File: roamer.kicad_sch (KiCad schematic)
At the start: 1 part

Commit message: Adding testpoints to I2C, SPI, and signals
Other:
- added sheet Bus - SPI (bus-spi.kicad_sch)
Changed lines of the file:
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@@
+	)
+	(sheet
+		(at 234.95 45.72)
+		(size 12.7 15.24)
+		(stroke
+			(width 0.1524)
+			(type solid)
+		)
+		(fill
+			(color 0 0 0 0.0000)
+		)
+		(property "Sheetname" "Bus - SPI"
+			(at 235.966 44.958 0)
+			(effects
+				(font
+					(size 1.27 1.27)
+				)
+				(justify left bottom)
+			)
+		)
+		(property "Sheetfile" "bus-spi.kicad_sch"
+			(at 248.2346 60.96 90)
+			(effects
+				(font
+					(size 1.27 1.27)
+				)
+				(justify left top)
+				(hide yes)
+			)
+		)
+		(pin "I2C{SCL SDA}" bidirectional
+			(at 241.3 60.96 270)
+			(effects
+				(font
+					(size 1.27 1.27)
+				)
+				(justify left)
+			)
+		)
+		(instances
+			(project "roamer"
+				(path "/1c59de6a-87fe-4223-8898-4b0383164a31"
+					(page "17")
+				)
+			)
+		)
 	)
 	(sheet

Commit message: Fixing lots of ERC errors
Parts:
- removed RN1: 100K, Resistor_SMD:R_Array_Convex_4x1206, symbol Device:R_Network04_Split
- added R9: 100K, Resistor_THT:R_Array_SIP8, symbol Device:R_Pack04_SIP_Split
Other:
- sheet Bus - SPI ports: added SPI{SCK MOSI MISO}; removed I2C{SCL SDA}
- sheet MCU ports: added AIRQ_SET, ~{AIRQ_RESET}; removed none

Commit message: Starting layout
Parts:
- R9: footprint Resistor_THT:R_Array_SIP8 -> Resistor_SMD:R_Array_Convex_4x1206
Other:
- sheet Interface - uSD ports: added none; removed uSD_DETECT
- sheet MCU ports: added SPI{SCK MISO MOSI}; removed SPI{CLK MISO MOSI}
- moved on the sheet: R9D

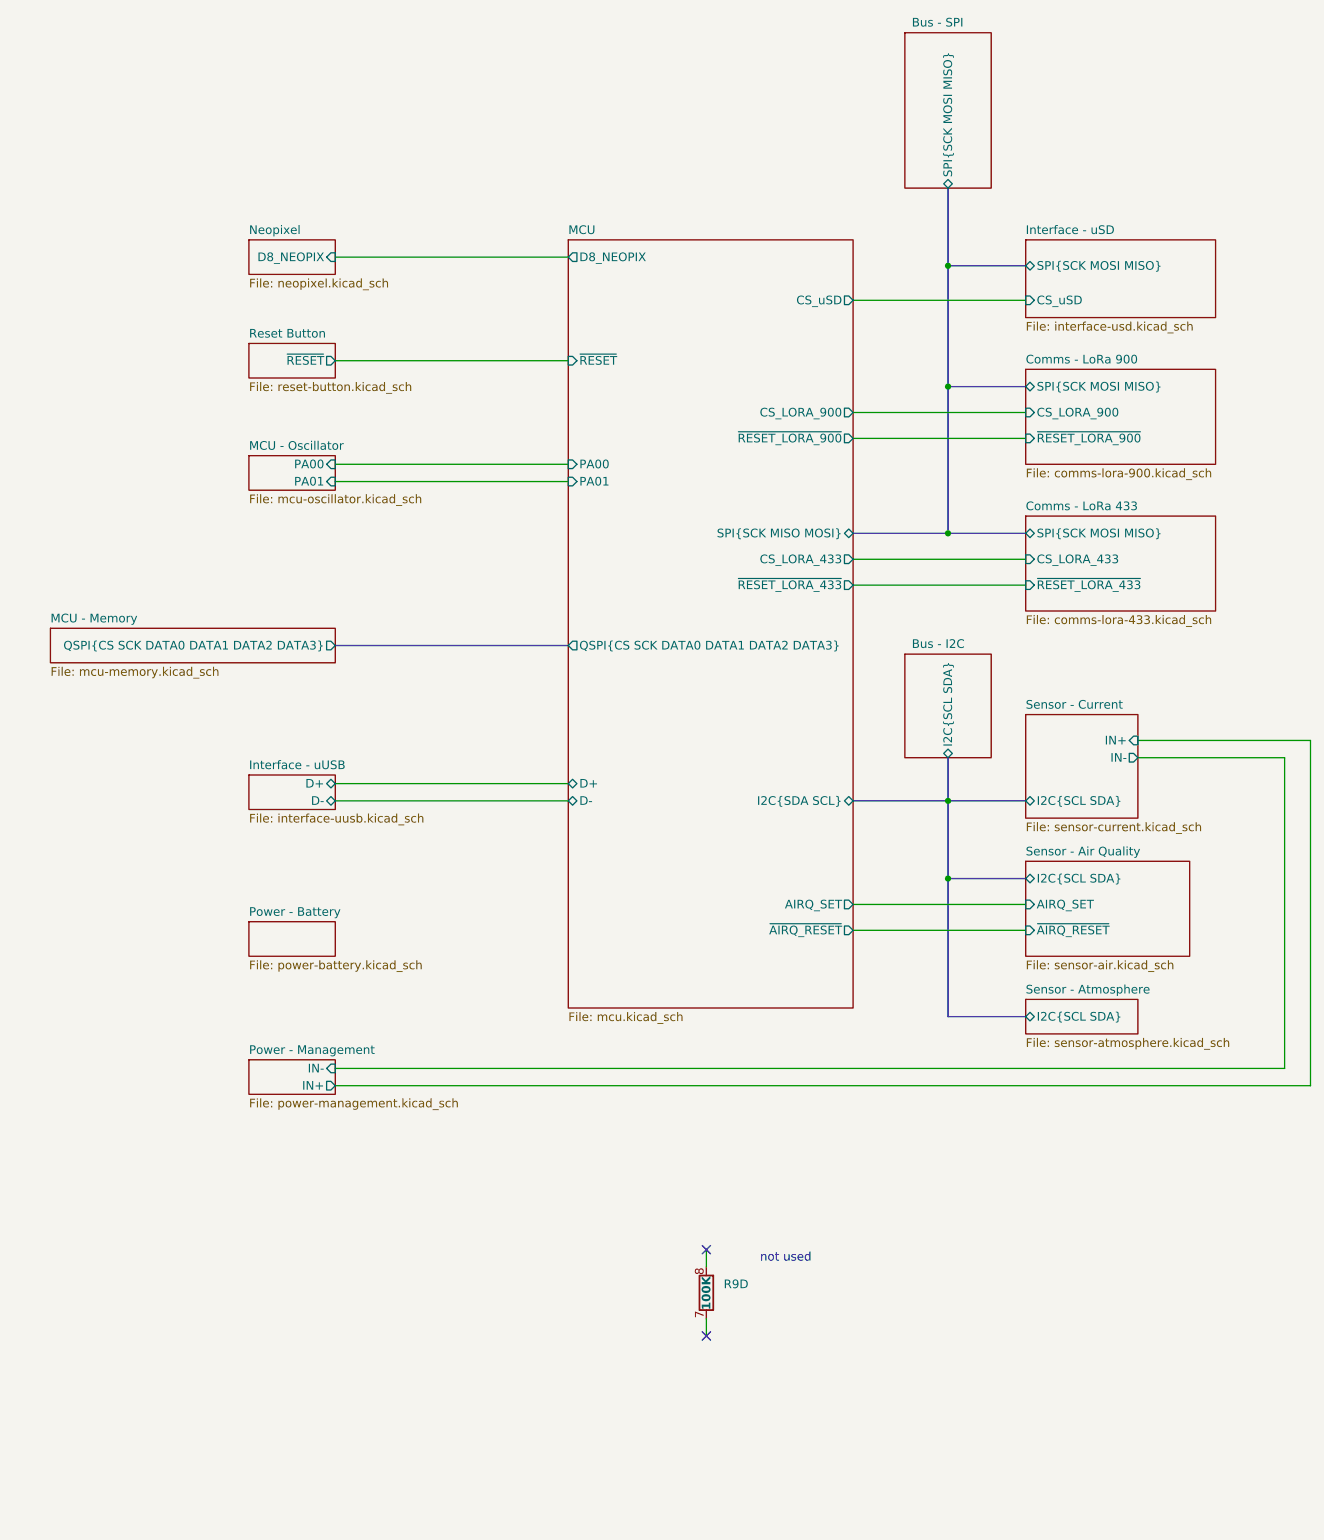
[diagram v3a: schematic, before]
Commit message: Added mounting holes
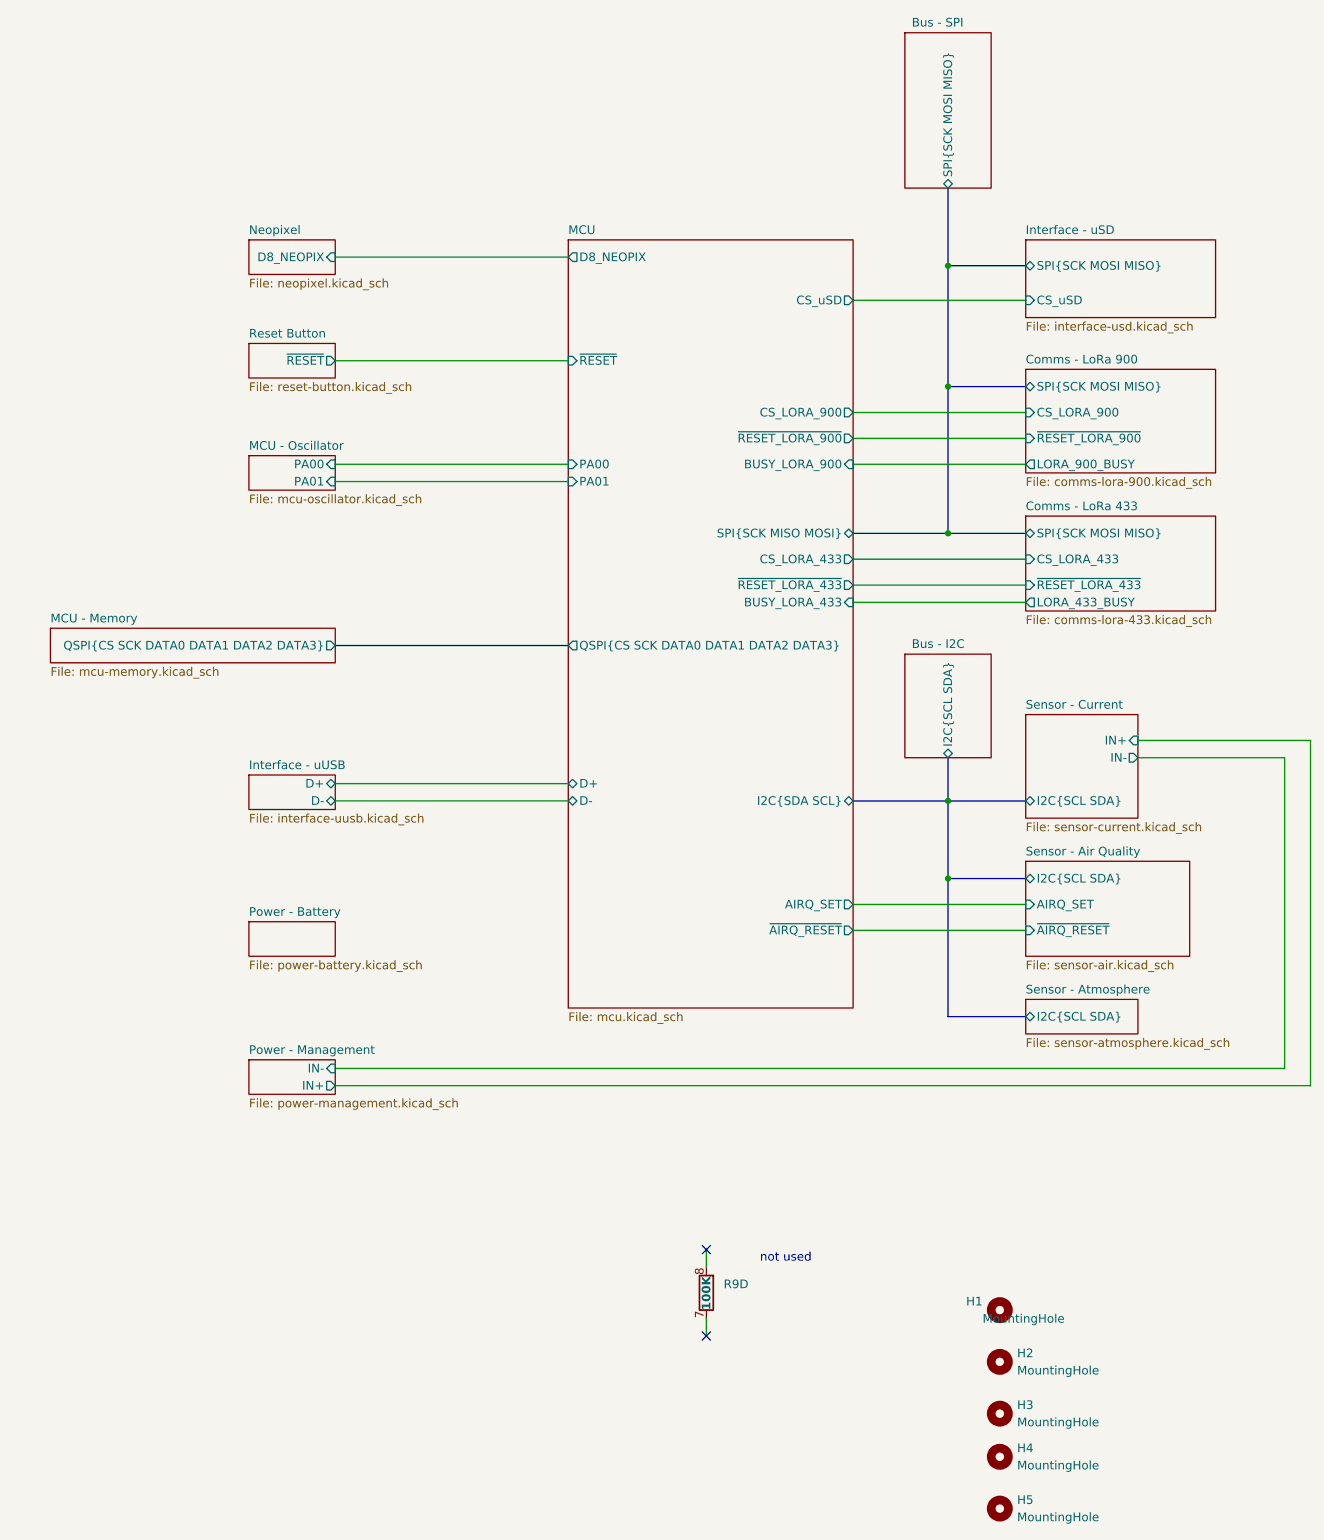
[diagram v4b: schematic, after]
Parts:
- added H1, H2, H3, H4, H5: MountingHole, MountingHole:MountingHole_2.2mm_M2_DIN965_Pad, symbol Mechanical:MountingHole
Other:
- sheet Comms - LoRa 433 ports: added LORA_433_BUSY; removed none
- sheet Comms - LoRa 900 ports: added LORA_900_BUSY; removed none
- sheet MCU ports: added BUSY_LORA_433, BUSY_LORA_900; removed none

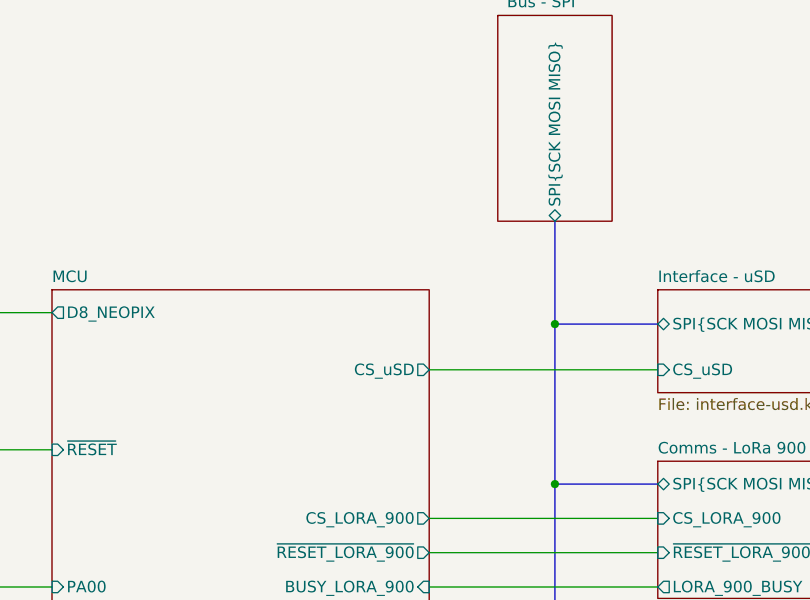
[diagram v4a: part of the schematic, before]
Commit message: Cleaning up traces
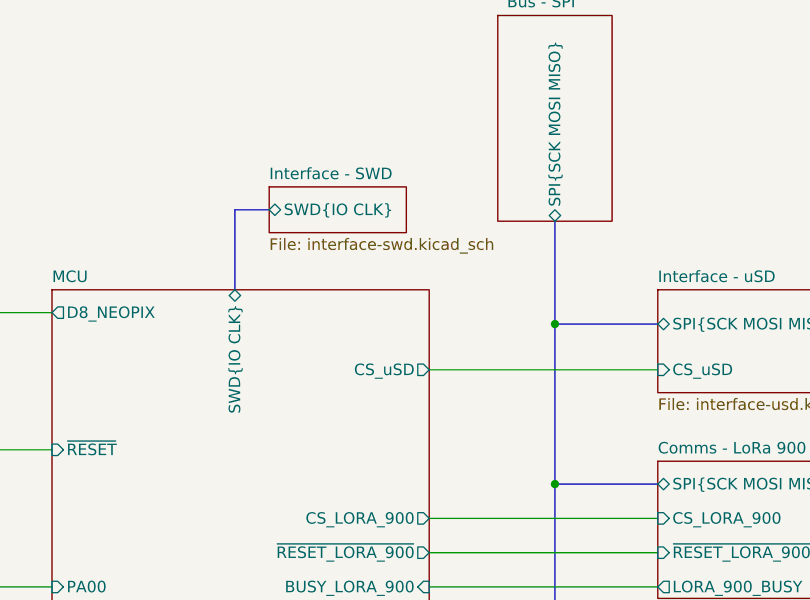
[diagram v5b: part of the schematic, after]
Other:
- added sheet Interface - SWD (interface-swd.kicad_sch)
- sheet MCU ports: added SWD{IO CLK}; removed none
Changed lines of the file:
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@@
 	(bus
 		(pts
+			(xy 205.74 68.58) (xy 205.74 59.69)
+		)
+		(stroke
+			(width 0)
+			(type default)
+		)
+	)
+	(bus
+		(pts
 			(xy 227.33 111.76) (xy 241.3 111.76)
 		)
@@
 	(bus
 		(pts
+			(xy 205.74 59.69) (xy 209.55 59.69)
+		)
+		(stroke
+			(width 0)
+			(type default)
+		)
+	)
+	(bus
+		(pts
 			(xy 252.73 182.88) (xy 241.3 182.88)
 		)
@@
 			(project "roamer"
 				(path "/1c59de6a-87fe-4223-8898-4b0383164a31"
-					(page "15")
+					(page "16")
 				)
 			)
@@
 			(project "roamer"
 				(path "/1c59de6a-87fe-4223-8898-4b0383164a31"
-					(page "12")
+					(page "13")
 				)
 			)
@@
 			(project "roamer"
 				(path "/1c59de6a-87fe-4223-8898-4b0383164a31"
-					(page "14")
+					(page "15")
 				)
 			)
@@
 			(project "roamer"
 				(path "/1c59de6a-87fe-4223-8898-4b0383164a31"
-					(page "11")
+					(page "12")
 				)
 			)
@@
 			(project "roamer"
 				(path "/1c59de6a-87fe-4223-8898-4b0383164a31"
-					(page "13")
+					(page "14")
 				)
 			)
@@
 			)
 		)
+		(pin "SWD{IO CLK}" bidirectional
+			(at 205.74 68.58 90)
+			(effects
+				(font
+					(size 1.27 1.27)
+				)
+				(justify right)
+			)
+		)
 		(instances
 			(project "roamer"
@@
 			(project "roamer"
 				(path "/1c59de6a-87fe-4223-8898-4b0383164a31"
-					(page "16")
+					(page "17")
 				)
 			)
@@
 	)
 	(sheet
+		(at 209.55 57.15)
+		(size 15.24 5.08)
+		(fields_autoplaced yes)
+		(stroke
+			(width 0.1524)
+			(type solid)
+		)
+		(fill
+			(color 0 0 0 0.0000)
+		)
+		(property "Sheetname" "Interface - SWD"
+			(at 209.55 56.4384 0)
+			(effects
+				(font
+					(size 1.27 1.27)
+				)
+				(justify left bottom)
+			)
+		)
+		(property "Sheetfile" "interface-swd.kicad_sch"
+			(at 209.55 62.8146 0)
+			(effects
+				(font
+					(size 1.27 1.27)
+				)
+				(justify left top)
+			)
+		)
+		(pin "SWD{IO CLK}" bidirectional
+			(at 209.55 59.69 180)
+			(effects
+				(font
+					(size 1.27 1.27)
+				)
+				(justify left)
+			)
+		)
+		(instances
+			(project "roamer"
+				(path "/1c59de6a-87fe-4223-8898-4b0383164a31"
+					(page "11")
+				)
+			)
+		)
+	)
+	(sheet
 		(at 234.95 38.1)
 		(size 12.7 22.86)
@@
 			(project "roamer"
 				(path "/1c59de6a-87fe-4223-8898-4b0383164a31"
-					(page "17")
+					(page "18")
 				)
 			)

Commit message: Creating fab package
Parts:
- R9: value 100K -> 4x 100K
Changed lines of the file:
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@@
 			)
 		)
-		(property "Value" "100K"
+		(property "Value" "4x 100K"
 			(at 205.74 226.06 90)
 			(effects

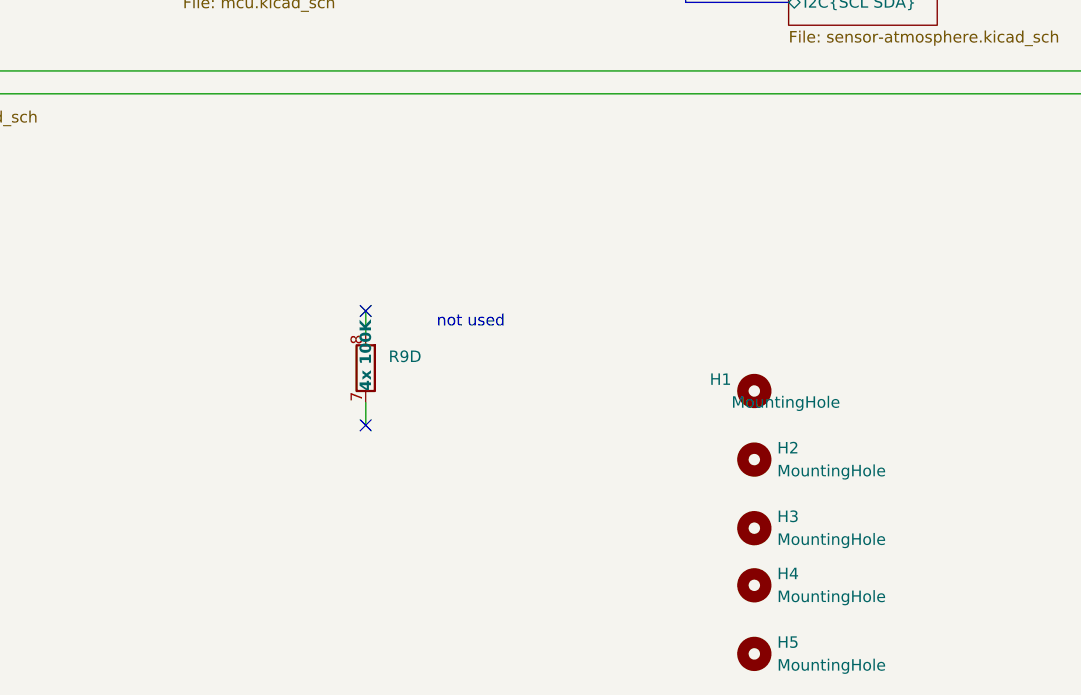
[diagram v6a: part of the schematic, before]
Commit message: Updating silkscreen comments
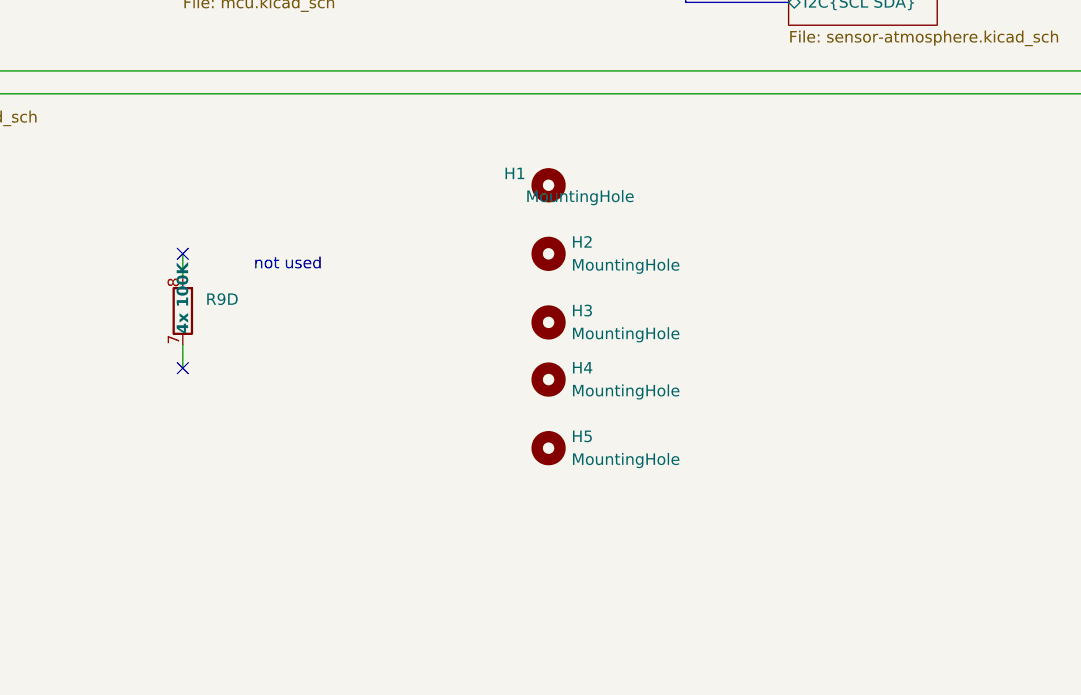
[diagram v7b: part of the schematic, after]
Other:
- moved on the sheet: H1, H2, H3, H4, H5, R9D
